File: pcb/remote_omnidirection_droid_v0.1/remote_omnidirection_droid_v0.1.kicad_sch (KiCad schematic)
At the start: 54 parts, among them J1 USB_C_Receptacle_USB2.0, J2 Conn_01x04, J3 BATT_CONNECT, J4 Conn_01x04, J5 Conn_01x04, M1 Motor_DC_ALT, M2 Motor_DC_ALT, M3 Motor_DC_ALT, Q1 BC846BS, SW1 SW_SPST, SW2 SW_SPST, SW3 SW_SPDT, U1 AZ1117-3.3, U2 AZ1117-5.0, U3 USBLC6-2SC6, U4 ESP32-S3-WROOM-2-N32R8V, U5 PCA9685PW

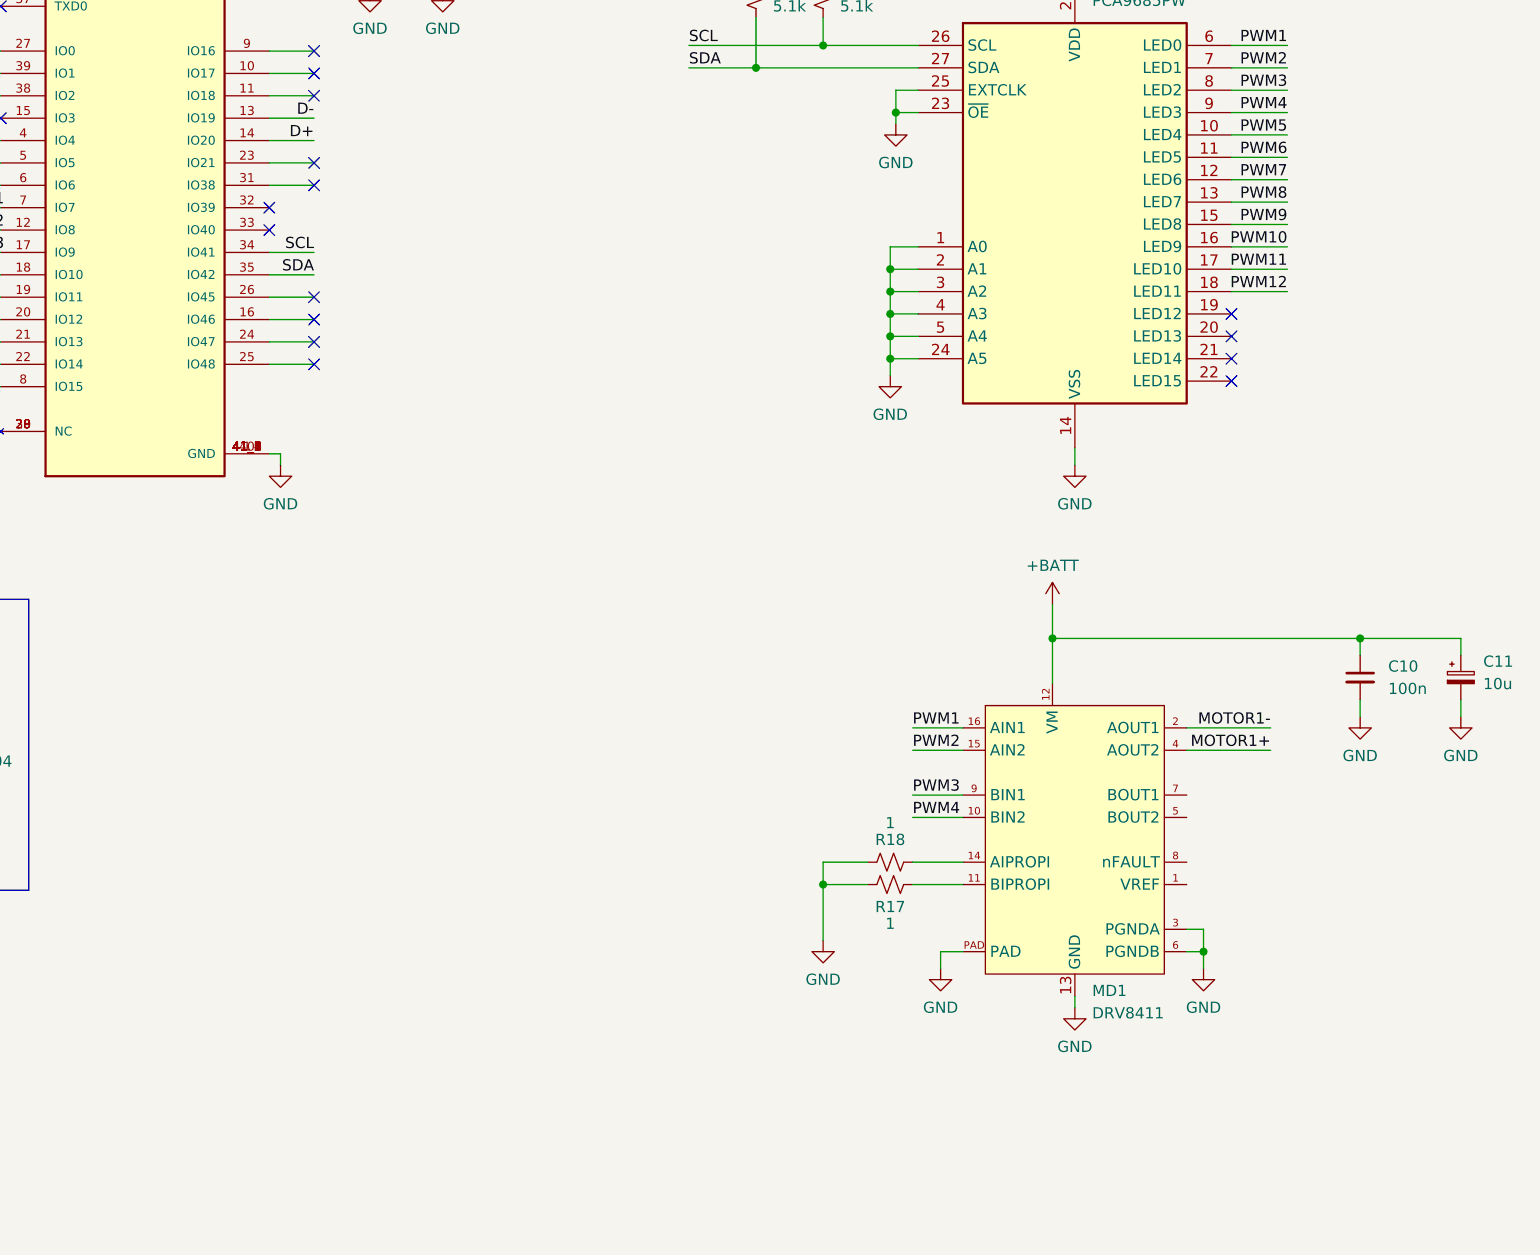
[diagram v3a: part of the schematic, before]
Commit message: added motor drivers
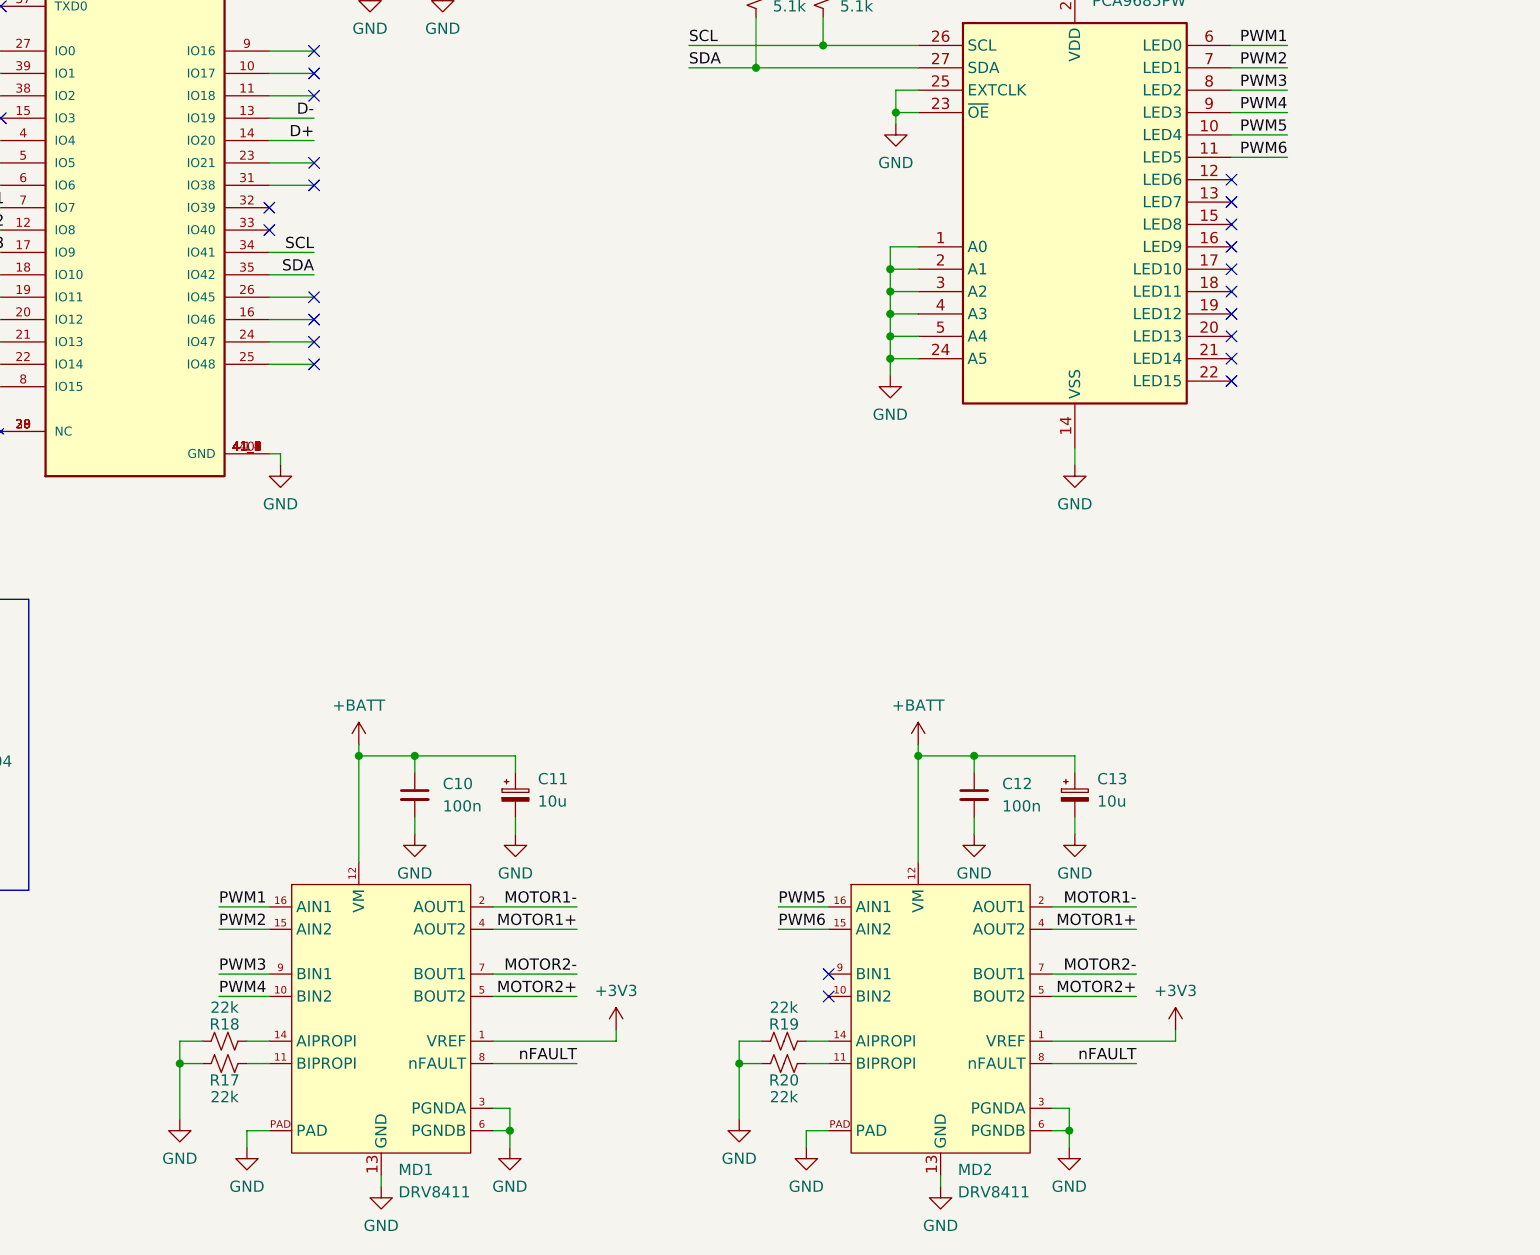
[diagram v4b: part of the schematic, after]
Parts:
- added C12: 100n, Capacitor_SMD:C_1206_3216Metric_Pad1.33x1.80mm_HandSolder, symbol Device:C_Small
- added C13: 10u, Capacitor_SMD:CP_Elec_5x5.3, symbol Device:C_Polarized_Small
- added MD2: DRV8411, Package_SO:HTSSOP-16-1EP_4.4x5mm_P0.65mm_EP3x3mm, symbol DroidSymbols:DRV8411
- added R19, R20: 22k, Resistor_SMD:R_1206_3216Metric_Pad1.30x1.75mm_HandSolder, symbol Device:R_Small_US
- C10: footprint (none) -> Capacitor_SMD:C_1206_3216Metric_Pad1.33x1.80mm_HandSolder
- C11: footprint (none) -> Capacitor_SMD:CP_Elec_5x5.3
- MD1: footprint (none) -> Package_SO:HTSSOP-16-1EP_4.4x5mm_P0.65mm_EP3x3mm
- R15, R16: footprint (none) -> Resistor_SMD:R_1206_3216Metric_Pad1.30x1.75mm_HandSolder
- R17, R18: value 1 -> 22k; footprint (none) -> Resistor_SMD:R_1206_3216Metric_Pad1.30x1.75mm_HandSolder
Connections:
- net +3V3: now also MD1.1 (VREF), MD2.1 (VREF)
- net +BATT: now also C12.1, C13.1, MD2.12 (VM)
- net GND: now also C12.2, C13.2, MD2.13 (GND), MD2.3 (PGNDA), MD2.6 (PGNDB), MD2.PAD, R19.2, R20.2
- net MOTOR1+: now also MD2.4 (AOUT2)
- net MOTOR1-: now also MD2.2 (AOUT1)
- net PWM5: now also MD2.16 (AIN1)
- net PWM6: now also MD2.15 (AIN2)
- net MOTOR2+: now reaches MD1.5 (BOUT2)
- net MOTOR2+: now also MD2.5 (BOUT2)
- net MOTOR2-: now reaches MD1.7 (BOUT1)
- net MOTOR2-: now also MD2.7 (BOUT1)
- net nFAULT: now reaches MD1.8 (nFAULT)
- net nFAULT: now also MD2.8 (nFAULT)
- net PWM10: no longer names the net of U5.16 (LED9)
- net PWM11: no longer names the net of U5.17 (LED10)
- net PWM12: no longer names the net of U5.18 (LED11)
- net PWM7: no longer names the net of U5.12 (LED6)
- net PWM8: no longer names the net of U5.13 (LED7)
- net PWM9: no longer names the net of U5.15 (LED8)
- new net: MD2.11 (BIPROPI), R20.1
- new net: MD2.14 (AIPROPI), R19.1
- no-connect marks 34 -> 42
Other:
- moved on the sheet: C10, C11, MD1, R17, R18

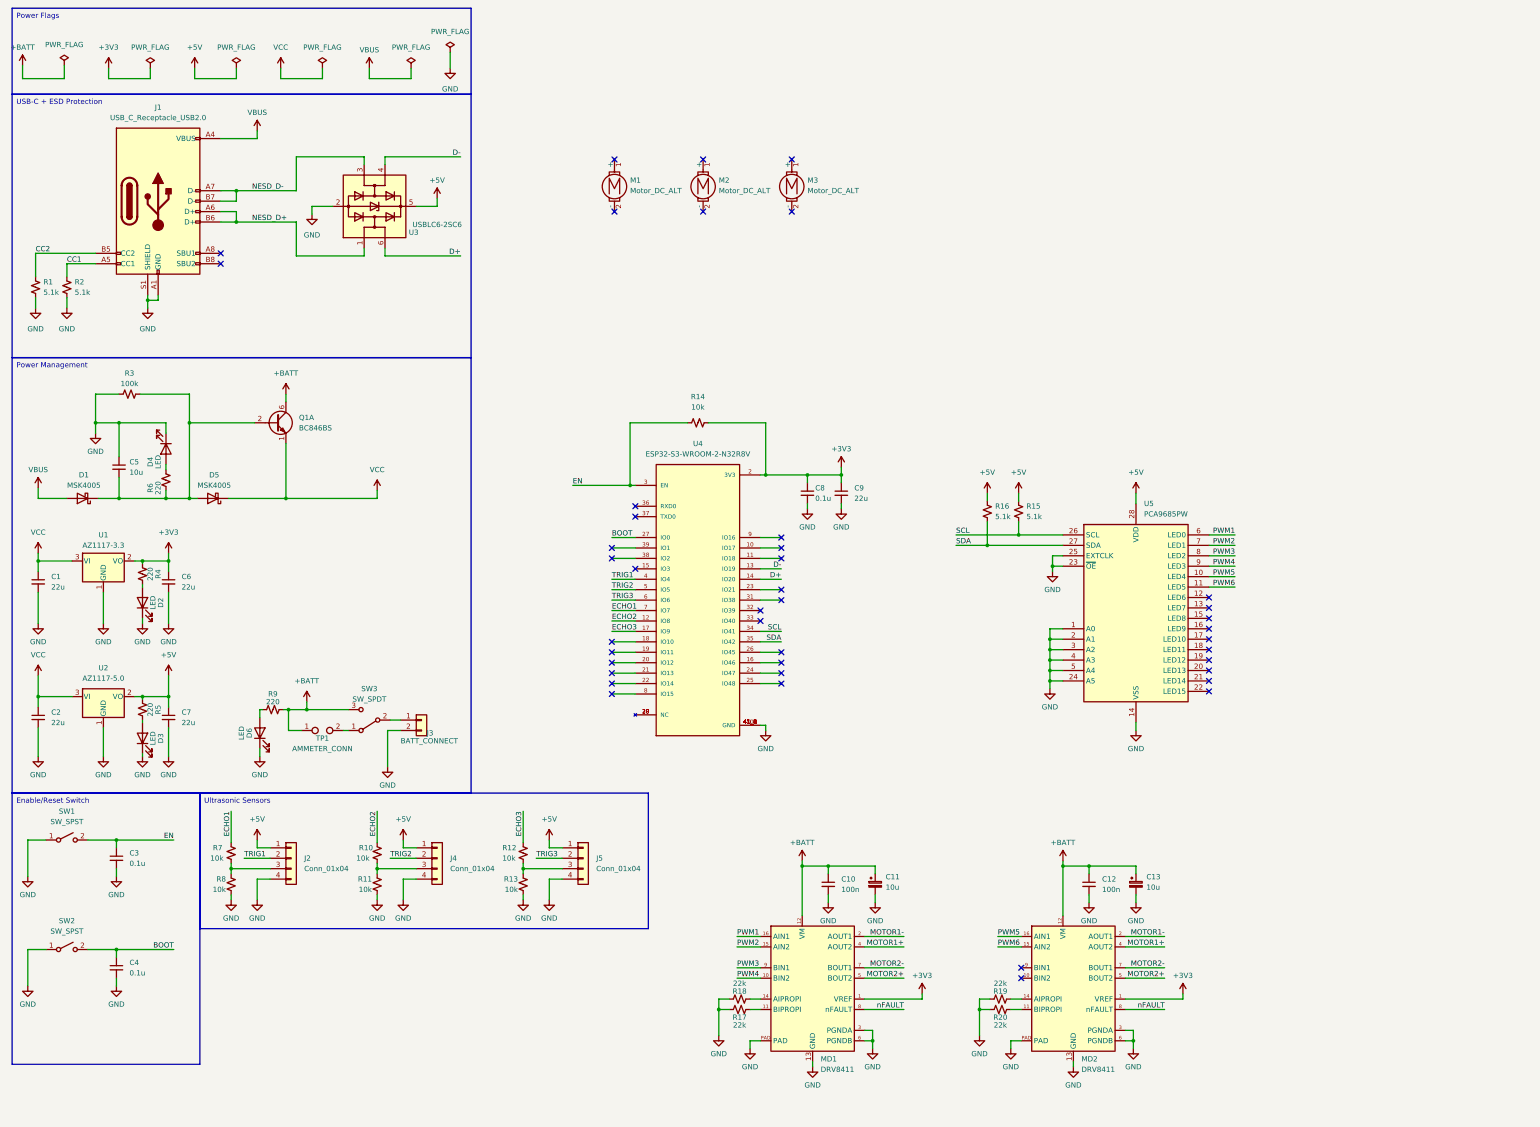
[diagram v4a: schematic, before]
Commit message: added BNO055
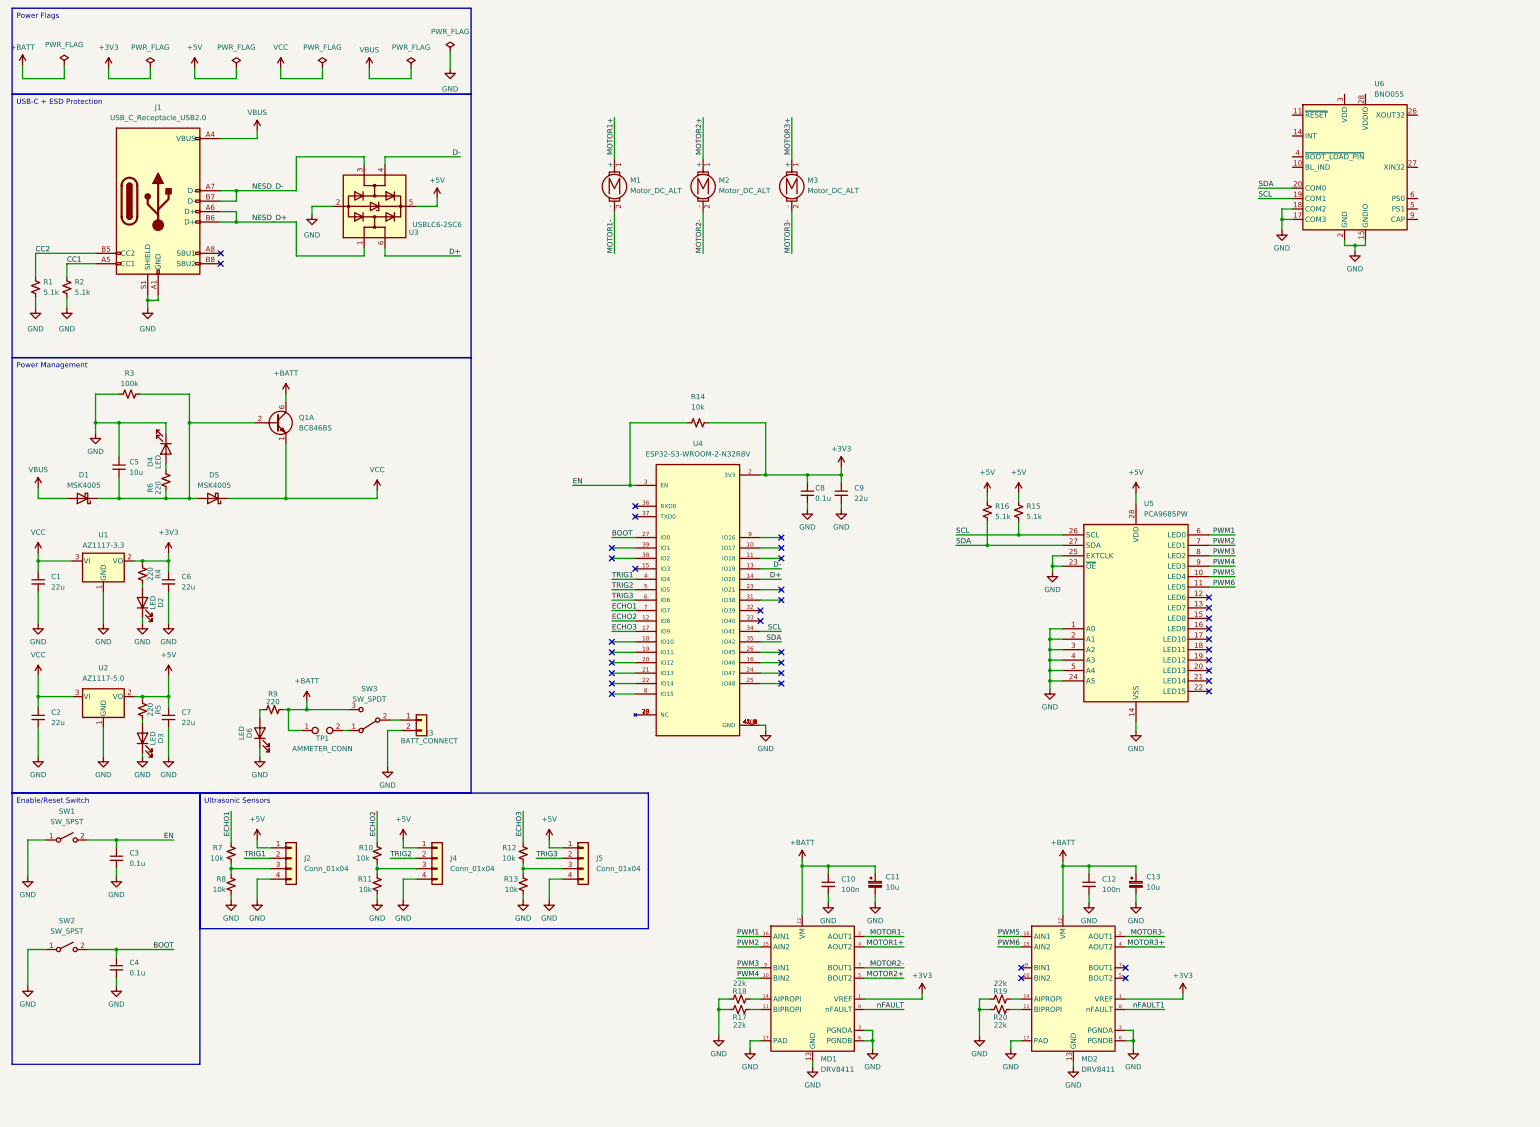
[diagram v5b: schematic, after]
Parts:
- added U6: BNO055, Package_LGA:LGA-28_5.2x3.8mm_P0.5mm, symbol Sensor_Motion:BNO055
- MD1, MD2: footprint Package_SO:HTSSOP-16-1EP_4.4x5mm_P0.65mm_EP3x3mm -> Drone_Footprints:PWP0016C-IPC_A
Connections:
- net GND: now also MD1.17 (PAD), MD2.17 (PAD), U6.15 (GNDIO), U6.16 (GNDIO), U6.17 (COM3), U6.18 (COM2), U6.2 (GND), U6.25 (GNDIO); no longer MD1.PAD, MD2.PAD
- net MOTOR1+: now also M1.1 (+); no longer MD2.4 (AOUT2)
- net MOTOR1-: now also M1.2 (-); no longer MD2.2 (AOUT1)
- net MOTOR2+: now also M2.1 (+); no longer MD2.5 (BOUT2)
- net MOTOR2-: now also M2.2 (-); no longer MD2.7 (BOUT1)
- net SCL: now also U6.19 (COM1)
- net SDA: now also U6.20 (COM0)
- net nFAULT: no longer MD2.8 (nFAULT)
- net MOTOR3+: now reaches M3.1 (+)
- net MOTOR3+: now also MD2.4 (AOUT2)
- net MOTOR3-: now reaches M3.2 (-)
- net MOTOR3-: now also MD2.2 (AOUT1)
- new net nFAULT1: MD2.8 (nFAULT)
- no-connect marks 42 -> 38

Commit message: board "complete"
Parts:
- added C14, C15: 22u, Capacitor_SMD:C_1206_3216Metric_Pad1.33x1.80mm_HandSolder, symbol Device:C_Small
- added C16, C17: 0.1u, Capacitor_SMD:C_1206_3216Metric_Pad1.33x1.80mm_HandSolder, symbol Device:C_Small
- added C18: 10u, Capacitor_SMD:C_1206_3216Metric_Pad1.33x1.80mm_HandSolder, symbol Device:C_Small
- added R21, R22: 10k, Resistor_SMD:R_1206_3216Metric_Pad1.30x1.75mm_HandSolder, symbol Device:R_Small_US
- added R23: 200k, Resistor_SMD:R_1206_3216Metric_Pad1.30x1.75mm_HandSolder, symbol Device:R_Small_US
- added U7: PCA9306D, Package_SO:SO-8_3.9x4.9mm_P1.27mm, symbol Interface:PCA9306D
- added Y1: 32.768kHz, Crystal:Crystal_SMD_Abracon_ABS25-4Pin_8.0x3.8mm, symbol Device:Crystal
- J1: footprint Connector_USB:USB_C_Receptacle_GCT_USB4085 -> Connector_USB:USB_C_Receptacle_GCT_USB4105-xx-A_16P_TopMnt_Horizontal
- R15, R16: value 5.1k -> 10k
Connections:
- net +3V3: now also U6.28 (VDDIO), U6.3 (VDD), U6.4 (~{BOOT_LOAD_PIN}), C17.2, R21.1, R22.1, U7.2 (VREF1)
- net +5V: now also R23.1, U7.7 (VREF2)
- net CC1: now also R1.1; no longer R2.2
- net CC2: now also R2.1; no longer R1.2
- net GND: now also R1.2, R2.2, U6.5 (PS1), U6.6 (PS0), C14.2, C15.2, C16.2, C17.1, C18.2, U7.1 (GND); no longer R1.1, R2.1
- net SCL: now also R22.2, U7.3 (SCL1); no longer R15.2, U5.26 (SCL)
- net SDA: now also R21.2, U7.4 (SDA1); no longer R16.2, U5.27 (SDA)
- net at U6.26 (XOUT32): now also C14.1, Y1.2
- net at U6.27 (XIN32): now also C15.1, Y1.1
- net at U6.9 (CAP): now also C16.1
- new net: C18.1, R23.2, U7.8 (EN)
- new net SCL_5V: R15.2, U5.26 (SCL), U7.6 (SCL2)
- new net SDA_5V: R16.2, U5.27 (SDA), U7.5 (SDA2)
- no-connect marks 38 -> 40
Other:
- moved on the sheet: C1, C2, C3, C4, C5, C6, C7, D1, D2, D3, D4, D5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

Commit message: near finalized v0.1
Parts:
- added BZ1: Buzzer, Buzzer_Beeper:Buzzer_12x9.5RM7.6, symbol Device:Buzzer
- added D3: 1N4148W, Diode_SMD:D_SOD-123, symbol Diode:1N4148W
- added H1, H2, H3, H4, H5, H6: MountingHole, MountingHole:MountingHole_2.7mm_M2.5, symbol Mechanical:MountingHole
- added IO15, IO16, IO17, IO18: TestPoint, TestPoint:TestPoint_THTPad_D2.5mm_Drill1.2mm, symbol Connector:TestPoint
- added J6: Conn_01x03, Connector_PinHeader_2.54mm:PinHeader_1x03_P2.54mm_Vertical, symbol Connector_Generic:Conn_01x03
- added Q1: 2N2219, Package_TO_SOT_THT:TO-92L_Inline, symbol Transistor_BJT:2N2219
- added R12: 180, Resistor_SMD:R_1206_3216Metric_Pad1.30x1.75mm_HandSolder, symbol Device:R_Small
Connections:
- net +5V: now also BZ1.1 (-), D3.1 (K), J6.2 (Pin_2)
- net GND: now also J6.1 (Pin_1), Q1.1 (E)
- net IO17: now reaches U4.10 (IO17)
- net IO17: now also IO17.1
- net IO18: now reaches U4.11 (IO18)
- net IO18: now also IO18.1
- net BUZZER: now reaches U4.18 (IO10)
- net BUZZER: now also R12.1
- net NeoPixel: now reaches U4.39 (IO1)
- net NeoPixel: now also J6.3 (Pin_3)
- net IO15: now reaches U4.8 (IO15)
- net IO15: now also IO15.1
- net IO16: now reaches U4.9 (IO16)
- net IO16: now also IO16.1
- net nFAULT: no longer names the net of MD1.8 (nFAULT)
- net nFAULT1: no longer names the net of MD2.8 (nFAULT)
- new net: BZ1.2 (+), D3.2 (A), Q1.3 (C)
- new net: Q1.2 (B), R12.2
- no-connect marks 40 -> 37
